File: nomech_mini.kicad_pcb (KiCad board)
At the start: 2 copper layers, 63 x 63 mm, 5 parts

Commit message: trying out LED position
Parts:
- added SM0603: Val**, SM0603, F.Cu at (138.1, 83.7)
- added SM0603: Val**, SM0603, F.Cu at (138.1, 95.8)
- added SM0603: Val**, SM0603, F.Cu at (150.3, 95.8)
- added SM0603: Val**, SM0603, F.Cu at (150.3, 83.7)

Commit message: starting schematic, adjusting pcb
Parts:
- added 80x80: 80mm, dp_pcb-DP8080_V1_drawing, F.Cu at (98.8, 154.8)
- DP10080_v1: renamed from 80mm; value 100mm -> 100x80mm
- moved MICRO-B_USB 95.6 mm to (80.2, 114.8), turned to 270 degrees
- moved TQFP44 70.4 mm to (96.2, 114.8)
- moved SM0603 31.0 mm to (107.1, 83.1)
- moved cap-electrode_10mm 31.0 mm to (113.2, 89.2)
- moved SM0603 31.0 mm to (107.1, 95.4)
- moved SM0603 30.9 mm to (119.4, 83.1)
- moved SM0603 30.9 mm to (119.4, 95.4)

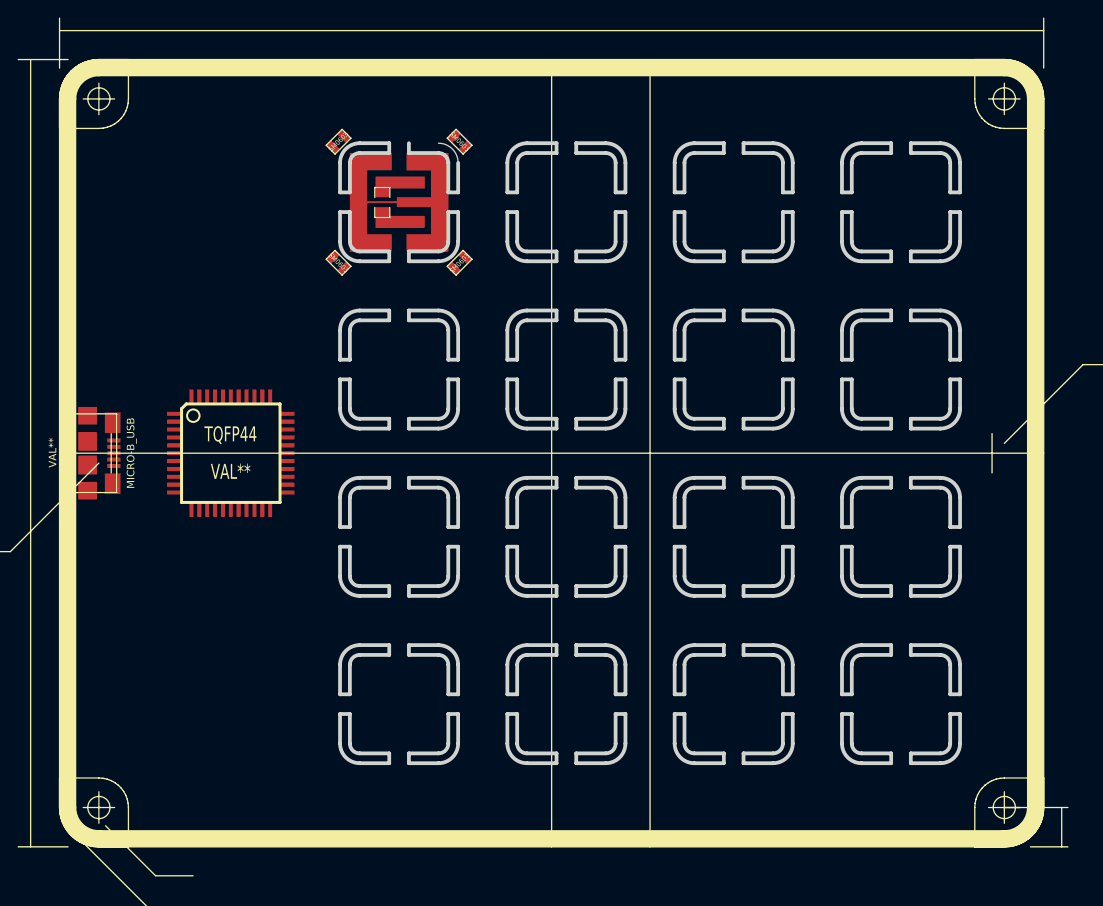
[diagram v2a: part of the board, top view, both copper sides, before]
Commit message: starting LED array, adjusting PCB
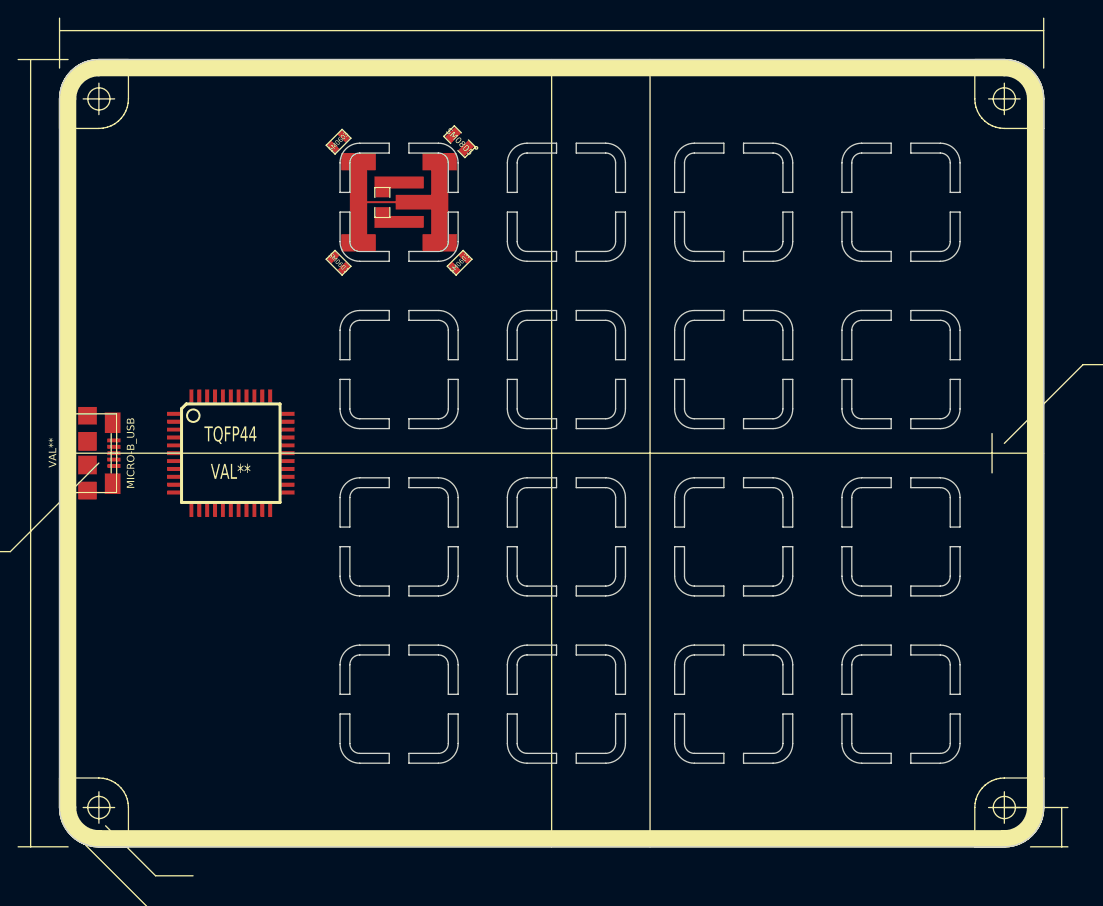
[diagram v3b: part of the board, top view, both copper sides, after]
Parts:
- SM0805: renamed from SM0603; footprint SM0603 -> SM0805
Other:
- board size 63 x 63 mm -> 100 x 80 mm

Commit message: working mainly on LEDs
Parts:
- moved cap-electrode_10mm 0.13 mm to (113.3, 89.1)
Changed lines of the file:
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@@
     (22 B.Mask user)
     (23 F.Mask user)
-    (24 Dwgs.User user hide)
+    (24 Dwgs.User user)
     (25 Cmts.User user)
     (26 Eco1.User user)
@@
   )
   (module cap-electrode_10mm (layer Front)
-    (at 113.25 89.25)
+    (at 113.3 89.125)
     (attr smd)
     (fp_text reference cap-electrode_10mm (at 0.1 6.4) (layer B.SilkS)

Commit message: messing about with elctrode
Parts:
- added cap-electrode_10mm: , cap-electrode_10mm, F.Cu at (113.1, 106.2)
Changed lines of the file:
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@@
     (tracks 0)
     (zones 0)
-    (modules 10)
+    (modules 11)
     (nets 1)
   )
@@
     (attr smd)
     (fp_text reference cap-electrode_10mm (at 0.1 6.4) (layer B.SilkS)
+      (effects (font (size 1.27 1.27) (thickness 0.0889)))
+    )
+    (fp_text value "" (at 0 0) (layer F.SilkS)
+      (effects (font (size 0.0004 0.0004) (thickness 0.00012)))
+    )
+    (fp_line (start -0.943 0.533) (end -0.943 1.549) (layer F.SilkS) (width 0.127))
+    (fp_line (start -0.943 1.549) (end -2.467 1.549) (layer F.SilkS) (width 0.127))
+    (fp_line (start -2.467 1.549) (end -2.467 0.533) (layer F.SilkS) (width 0.127))
+    (fp_line (start -2.467 -0.483) (end -2.467 -1.499) (layer F.SilkS) (width 0.127))
+    (fp_line (start -2.467 -1.499) (end -0.943 -1.499) (layer F.SilkS) (width 0.127))
+    (fp_line (start -0.943 -1.499) (end -0.943 -0.483) (layer F.SilkS) (width 0.127))
+    (pad 1 smd rect (at 4.125 4.125) (size 3.5 1.75)
+      (layers Front F.Mask)
+      (clearance 0.1)
+    )
+    (pad 1 smd rect (at 4.125 -4.125) (size 3.5 1.75)
+      (layers Front F.Mask)
+      (clearance 0.1)
+    )
+    (pad 1 smd rect (at -4.125 4.125) (size 3.5 1.75)
+      (layers Front F.Mask)
+      (clearance 0.1)
+    )
+    (pad 1 smd rect (at -4.125 0) (size 1.75 8.2)
+      (layers Front F.SilkS F.Mask)
+    )
+    (pad 1 smd rect (at 4.125 0) (size 1.75 8.2)
+      (layers Front F.SilkS F.Mask)
+    )
+    (pad 1 smd oval (at -4.125 -4.125) (size 1.75 1.75)
+      (layers Front F.Mask)
+    )
+    (pad 1 smd rect (at 2.15 0) (size 5 1.5)
+      (layers Front F.Mask)
+    )
+    (pad 2 smd rect (at 0 -2) (size 5 1.22)
+      (layers Front F.Mask)
+    )
+    (pad 2 smd rect (at 0 2) (size 5 1.22)
+      (layers Front F.Mask)
+    )
+    (pad 1 smd rect (at -1.45 0) (size 4.25 0.2)
+      (layers Front F.Mask)
+      (clearance 0.1)
+    )
+    (pad 2 smd rect (at -1.7 -0.95 90) (size 0.889 1.397)
+      (layers Front F.Paste F.Mask)
+    )
+    (pad 2 smd rect (at -1.7 0.95 90) (size 0.889 1.397)
+      (layers Front F.Paste F.Mask)
+    )
+    (pad 1 smd rect (at -4.125 -4.125) (size 3.5 1.75)
+      (layers Front F.Mask)
+      (clearance 0.1)
+    )
+    (pad 1 smd oval (at -4.125 4.125) (size 1.75 1.75)
+      (layers Front F.Mask)
+    )
+    (pad 1 smd oval (at 4.125 -4.125) (size 1.75 1.75)
+      (layers Front F.Mask)
+    )
+    (pad 1 smd oval (at 4.125 4.125) (size 1.75 1.75)
+      (layers Front F.Mask)
+    )
+  )
+  (module cap-electrode_10mm (layer Front)
+    (at 113.075 106.15)
+    (attr smd)
+    (fp_text reference cap-electrode_10mm (at 0.1 6.4) (layer B.SilkS)

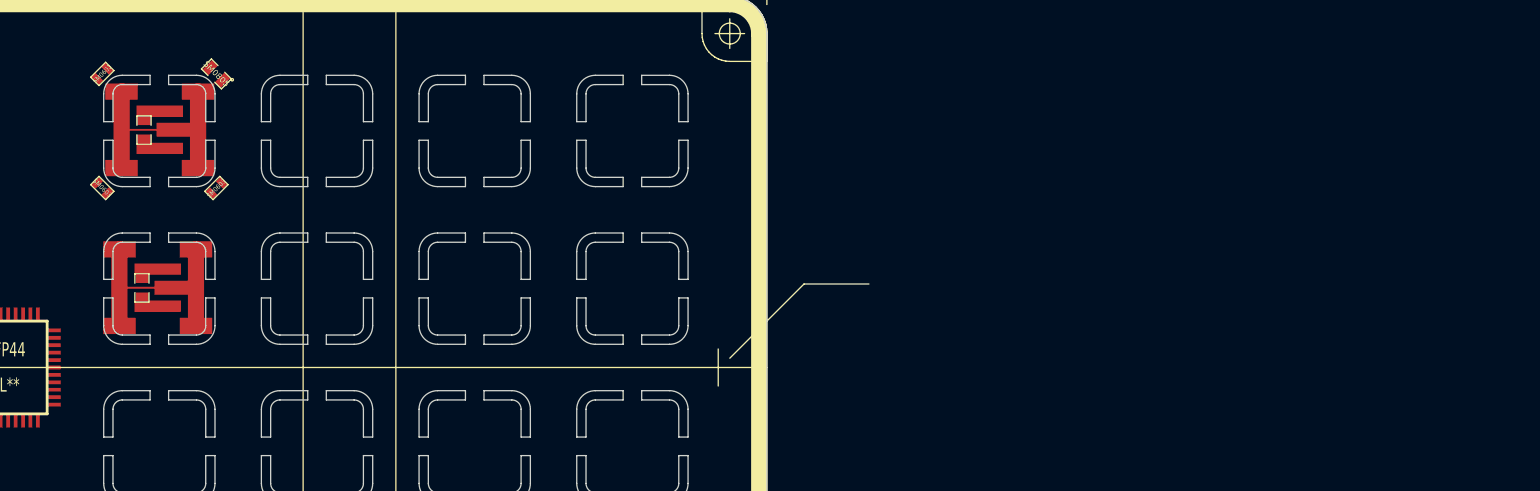
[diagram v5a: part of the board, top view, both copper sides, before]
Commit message: adding netlist, just for messing with footprints
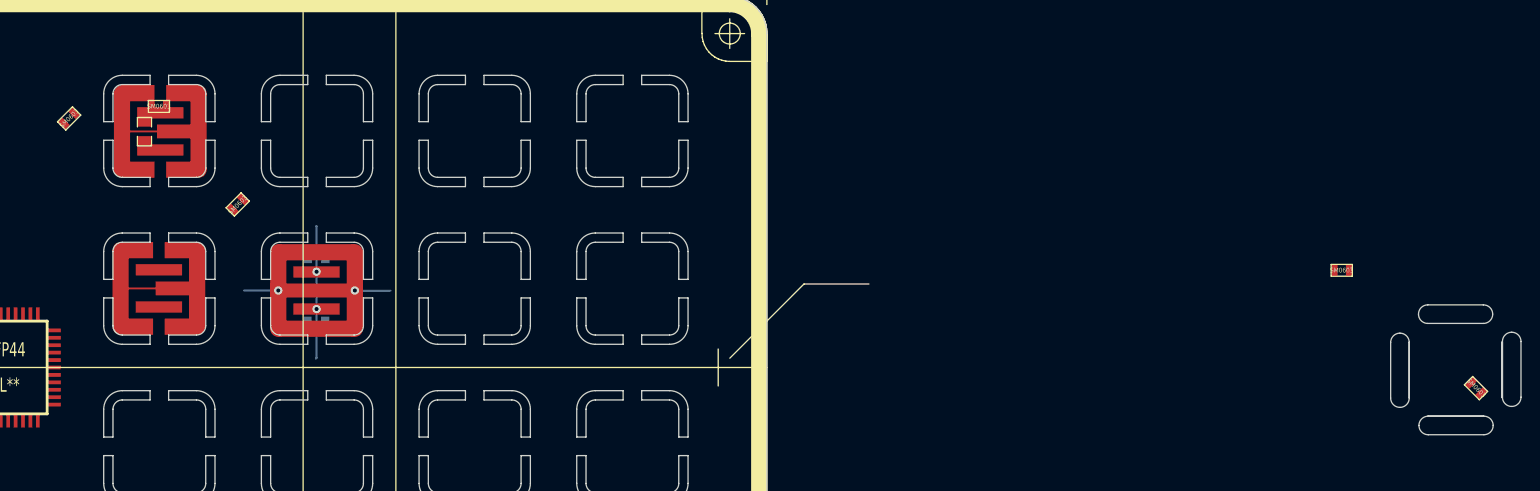
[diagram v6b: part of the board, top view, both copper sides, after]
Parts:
- removed the SM0603 at (107.1, 83.1)
- removed the SM0603 at (119.4, 95.4)
- removed the cap-electrode_10mm at (113.3, 89.1)
- removed the cap-electrode_10mm at (113.1, 106.2)
- added R4: R, cap-electrode_10mm_2layer, F.Cu at (130.2, 106.5)
- added SM0603: Val**, SM0603, F.Cu at (255.2, 117.0)
- added SM0603: Val**, SM0603, F.Cu at (113.2, 86.6)
- added SM0603: Val**, SM0603, F.Cu at (240.7, 104.3)
- added SM0603: Val**, SM0603, F.Cu at (121.7, 97.2)
- added SM0805: Val*, SM0805, B.Cu at (130.2, 102.8)
- added cap-electrode_10mm: , cap-electrode_10mm, F.Cu at (113.3, 89.3)
- added cap-electrode_10mm_2layer: , cap-electrode_10mm_2layer, F.Cu at (113.2, 106.2)
- SM0805: moved to B.Cu
- moved SM0805 29.0 mm to (130.2, 110.0), turned to 0 degrees
- moved SM0603 8.31 mm to (103.5, 87.9), turned to 225 degrees
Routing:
- net N-0000016: track 0.00 -> 44.7 mm, vias 0 -> 2
- net N-0000017: track 0.00 -> 14.4 mm, vias 0 -> 2
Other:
- board size 100 x 80 mm -> 152.8 x 63 mm

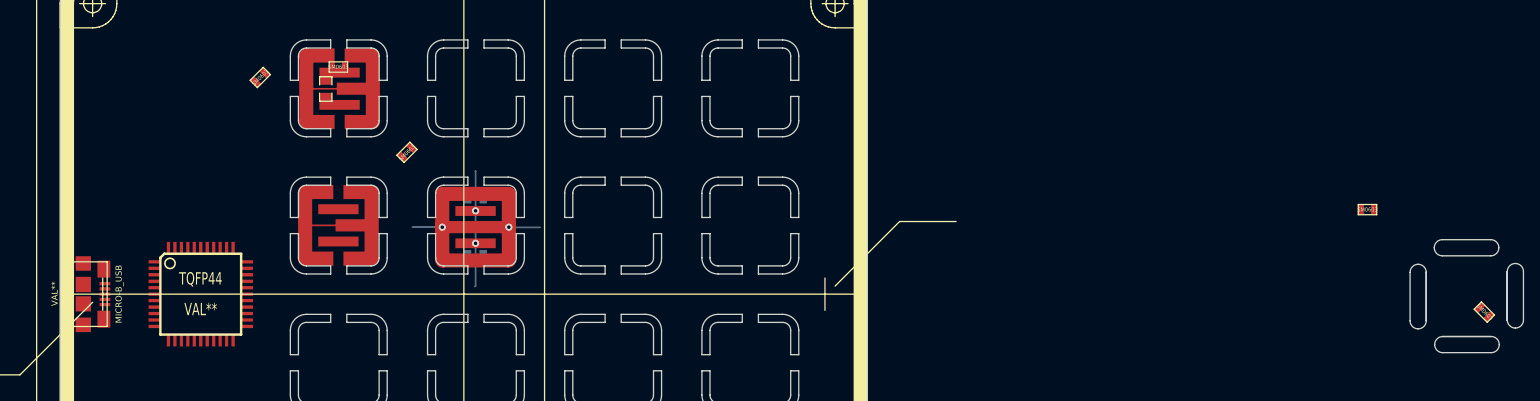
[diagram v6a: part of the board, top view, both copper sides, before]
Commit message: commiting before change to LED numbers
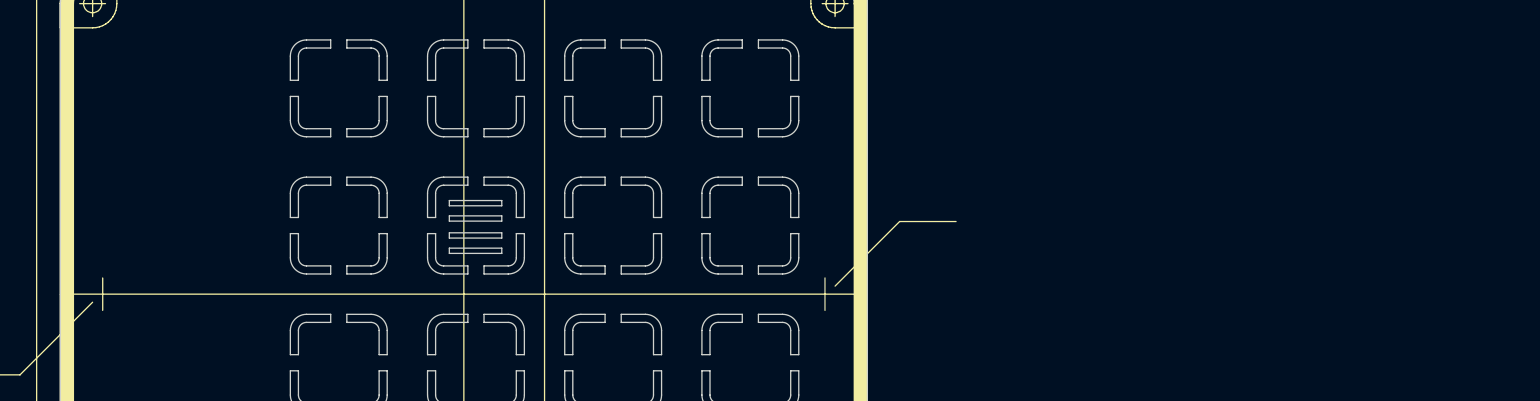
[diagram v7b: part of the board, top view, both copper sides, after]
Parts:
- removed MICRO-B_USB: VAL**, MICRO-B_USB
- removed R4: R, cap-electrode_10mm_2layer
- removed SM0603 (x5): Val**, SM0603
- removed SM0805: Val**, SM0805
- removed SM0805: Val*, SM0805
- removed TQFP44: VAL**, TQFP44
- removed cap-electrode_10mm: , cap-electrode_10mm
- removed cap-electrode_10mm_2layer: , cap-electrode_10mm_2layer
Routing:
- net N-0000016: track 44.7 -> 0.00 mm, vias 2 -> 0
- net N-0000017: track 14.4 -> 0.00 mm, vias 2 -> 0
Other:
- board size 152.8 x 63 mm -> 100 x 80 mm

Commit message: starting layout
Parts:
- removed STUB: VAL**, STUB
- added C1: 100nF, SM0805, B.Cu at (75.2, 225.6)
- added C10: 100nF, SM0805, B.Cu at (108.1, 225.6)
- added C11: 10nF, SM0805, B.Cu at (68.0, 225.6)
- added C12: 18pF, SM0805, B.Cu at (89.8, 225.6)
- added C13: 10nF, SM0805, B.Cu at (71.6, 225.6)
- added C14: 100nF, SM0805, B.Cu at (140.9, 225.6)
- added C15: 4.7nF, SM0805, B.Cu at (151.8, 225.2)
- added C16: 4.7nF, SM0805, B.Cu at (228.5, 225.9)
- added C17: 4.7nF, SM0805, B.Cu at (184.7, 225.9)
- added C18: 4.7nF, SM0805, B.Cu at (129.9, 225.6)
- added C2: 100nF, SM0805, B.Cu at (151.9, 222.8)
- added C3: 100nF, SM0805, B.Cu at (57.0, 225.6)
- added C4: 1uF, SM0805, B.Cu at (86.2, 225.6)
- added C5: 100nF, SM0805, B.Cu at (108.1, 227.9)
- added C6: 10nF, SM0805, B.Cu at (111.7, 225.6)
- added C7: 100nF, SM0805, B.Cu at (104.4, 225.6)
- added C8: 10nF, SM0805, B.Cu at (64.3, 225.6)
- added C9: 18pF, SM0805, B.Cu at (93.5, 225.6)
- added CON1: USB_2B, MICRO-B_USB, B.Cu at (139.2, 85.0)
- added CON2: AVR-ISP-6, pin_array_3x2, F.Cu at (164.0, 96.0)
- added D1: LED, KPJA-2107SURCK, B.Cu at (106.8, 111.2)
- added D10: LED, KPJA-2107SURCK, B.Cu at (71.8, 227.5)
- added D11: LED, KPJA-2107SURCK, B.Cu at (100.2, 227.5)
- added D12: LED, KPJA-2107SURCK, B.Cu at (81.3, 227.5)
- added D13: LED, KPJA-2107SURCK, B.Cu at (199.1, 242.2)
- added D14: LED, KPJA-2107SURCK, B.Cu at (227.6, 242.2)
- added D15: LED, KPJA-2107SURCK, B.Cu at (265.5, 242.2)
- added D16: LED, KPJA-2107SURCK, B.Cu at (213.3, 242.2)
- added D17: LED, KPJA-2107SURCK, B.Cu at (170.6, 242.2)
- added D18: LED, KPJA-2107SURCK, B.Cu at (76.5, 227.5)
- added D19: LED, KPJA-2107SURCK, B.Cu at (251.3, 242.2)
- added D2: LED, KPJA-2107SURCK, B.Cu at (120.8, 111.2)
- added D20: LED, KPJA-2107SURCK, B.Cu at (175.3, 242.2)
- added D21: LED, KPJA-2107SURCK, B.Cu at (203.8, 242.2)
- added D22: LED, KPJA-2107SURCK, B.Cu at (260.8, 242.2)
- added D23: LED, KPJA-2107SURCK, B.Cu at (246.5, 242.2)
- added D24: LED, KPJA-2107SURCK, B.Cu at (232.3, 242.2)
- added D25: LED, KPJA-2107SURCK, B.Cu at (218.1, 242.2)
- added D26: LED, KPJA-2107SURCK, B.Cu at (86.0, 227.5)
- added D27: LED, KPJA-2107SURCK, B.Cu at (90.8, 227.5)
- added D28: LED, KPJA-2107SURCK, B.Cu at (184.8, 242.2)
- added D29: LED, KPJA-2107SURCK, B.Cu at (222.8, 242.2)
- added D3: LED, KPJA-2107SURCK, B.Cu at (123.8, 125.2)
- added D30: LED, KPJA-2107SURCK, B.Cu at (67.0, 227.5)
- added D31: LED, KPJA-2107SURCK, B.Cu at (180.1, 242.2)
- added D32: LED, KPJA-2107SURCK, B.Cu at (241.8, 242.2)
- added D33: LED, KPJA-2107SURCK, B.Cu at (208.6, 242.2)
- added D4: LED, KPJA-2107SURCK, B.Cu at (137.8, 125.5)
- added D5: LED, KPJA-2107SURCK, B.Cu at (194.3, 242.2)
- added D6: LED, KPJA-2107SURCK, B.Cu at (256.0, 242.2)
- added D7: LED, KPJA-2107SURCK, B.Cu at (275.0, 242.2)
- added D8: LED, KPJA-2107SURCK, B.Cu at (189.6, 242.2)
- added D9: LED, KPJA-2107SURCK, B.Cu at (237.0, 242.2)
- added E1: CAP-ELECTRODE, cap-electrode_10mm_2layer, F.Cu at (113.8, 118.2)
- added E10: CAP-ELECTRODE, cap-electrode_10mm_2layer, F.Cu at (130.8, 152.2)
- added E11: CAP-ELECTRODE, cap-electrode_10mm_2layer, F.Cu at (147.8, 152.2)
- added E12: CAP-ELECTRODE, cap-electrode_10mm_2layer, F.Cu at (164.8, 152.2)
- added E13: CAP-ELECTRODE, cap-electrode_10mm_2layer, F.Cu at (113.8, 169.2)
- added E14: CAP-ELECTRODE, cap-electrode_10mm_2layer, F.Cu at (130.8, 169.2)
- added E15: CAP-ELECTRODE, cap-electrode_10mm_2layer, F.Cu at (147.8, 169.2)
- added E16: CAP-ELECTRODE, cap-electrode_10mm_2layer, F.Cu at (164.8, 169.2)
- added E2: CAP-ELECTRODE, cap-electrode_10mm_2layer, F.Cu at (130.8, 118.2)
- added E3: CAP-ELECTRODE, cap-electrode_10mm_2layer, F.Cu at (147.8, 118.2)
- added E4: CAP-ELECTRODE, cap-electrode_10mm_2layer, F.Cu at (164.8, 118.2)
- added E5: CAP-ELECTRODE, cap-electrode_10mm_2layer, F.Cu at (113.8, 135.2)
- added E6: CAP-ELECTRODE, cap-electrode_10mm_2layer, F.Cu at (130.8, 135.2)
- added E7: CAP-ELECTRODE, cap-electrode_10mm_2layer, F.Cu at (147.8, 135.2)
- added E8: CAP-ELECTRODE, cap-electrode_10mm_2layer, F.Cu at (164.8, 135.2)
- added E9: CAP-ELECTRODE, cap-electrode_10mm_2layer, F.Cu at (113.8, 152.2)
- added L1: FERRITE_BEAD, SM0805, B.Cu at (100.8, 225.6)
- added L2: FERRITE_BEAD, SM0805, B.Cu at (60.7, 225.6)
- added P2: CONN_1, PIN_ARRAY_1, F.Cu at (145.6, 208.1)
- added P3: CONN_1, PIN_ARRAY_1, F.Cu at (139.8, 208.1)
- added P4: CONN_1, PIN_ARRAY_1, F.Cu at (134.0, 208.1)
- added P5: CONN_1, PIN_ARRAY_1, F.Cu at (128.2, 208.1)
- added P6: CONN_1, PIN_ARRAY_1, F.Cu at (167.5, 102.8)
- added Q1: MOSFET_N, SOT23-NX7002AK, B.Cu at (166.6, 241.6)
- added Q2: MOSFET_N, SOT23-NX7002AK, B.Cu at (163.5, 241.6)
- added Q3: MOSFET_N, SOT23-NX7002AK, B.Cu at (157.2, 241.6)
- added Q4: MOSFET_N, SOT23-NX7002AK, B.Cu at (160.3, 241.6)
- added R1: 10k, SM0805, B.Cu at (97.1, 225.6)
- added R10: 1M, SM0805, B.Cu at (177.4, 225.9)
- added R11: 1M, SM0805, B.Cu at (144.6, 225.6)
- added R12: 1M, SM0805, B.Cu at (133.6, 225.6)
- added R13: 1k, SM0805, B.Cu at (159.1, 223.6)
- added R14: 1k, SM0805, B.Cu at (181.1, 225.9)
- added R15: 1k, SM0805, B.Cu at (148.2, 225.6)
- added R16: 1k, SM0805, B.Cu at (137.2, 225.6)
- added R17: 22R, SM0805, B.Cu at (206.6, 225.9)
- added R18: 22R, SM0805, B.Cu at (199.3, 225.9)
- added R19: 22R, SM0805, B.Cu at (224.8, 225.9)
- added R2: 22R, SM0805, B.Cu at (78.9, 225.6)
- added R20: 22R, SM0805, B.Cu at (192.0, 225.9)
- added R21: 4k7, SM0805, B.Cu at (210.2, 225.9)
- added R22: 4k7, SM0805, B.Cu at (202.9, 225.9)
- added R23: 4k7, SM0805, B.Cu at (188.3, 225.9)
- added R24: 4k7, SM0805, B.Cu at (195.7, 225.9)
- added R25: 120R, SM0805, B.Cu at (213.9, 225.9)
- added R26: 120R, SM0805, B.Cu at (173.8, 225.9)
- added R27: 120R, SM0805, B.Cu at (243.1, 225.9)
- added R28: 120R, SM0805, B.Cu at (257.6, 225.9)
- added R29: 120R, SM0805, B.Cu at (144.6, 227.9)
- added R3: 22R, SM0805, B.Cu at (82.5, 225.6)
- added R30: 120R, SM0805, B.Cu at (159.2, 225.9)
- added R31: 120R, SM0805, B.Cu at (111.8, 227.9)
- added R32: 120R, SM0805, B.Cu at (130.0, 227.9)
- added R33: 120R, SM0805, B.Cu at (217.5, 225.9)
- added R34: 120R, SM0805, B.Cu at (232.1, 225.9)
- added R35: 120R, SM0805, B.Cu at (246.7, 225.9)
- added R36: 120R, SM0805, B.Cu at (261.3, 225.9)
- added R37: 120R, SM0805, B.Cu at (170.1, 225.9)
- added R38: 120R, SM0805, B.Cu at (155.5, 225.9)
- added R39: 120R, SM0805, B.Cu at (140.9, 227.9)
- added R4: 120R, SM0805, B.Cu at (104.5, 227.9)
- added R40: 120R, SM0805, B.Cu at (126.3, 227.9)
- added R41: 120R, SM0805, B.Cu at (221.2, 225.9)
- added R42: 120R, SM0805, B.Cu at (235.8, 225.9)
- added R43: 120R, SM0805, B.Cu at (250.3, 225.9)
- added R44: 120R, SM0805, B.Cu at (264.9, 225.9)
- added R45: 120R, SM0805, B.Cu at (166.5, 225.9)
- added R46: 120R, SM0805, B.Cu at (115.4, 227.9)
- added R47: 120R, SM0805, B.Cu at (137.3, 227.9)
- added R48: 120R, SM0805, B.Cu at (122.7, 227.9)
- added R49: 120R, SM0805, B.Cu at (268.6, 225.9)
- added R5: 1k, SM0805, B.Cu at (126.3, 225.6)
- added R50: 120R, SM0805, B.Cu at (239.4, 225.9)
- added R51: 120R, SM0805, B.Cu at (254.0, 225.9)
- added R52: 120R, SM0805, B.Cu at (272.2, 225.9)
- added R53: 120R, SM0805, B.Cu at (162.8, 225.9)
- added R54: 120R, SM0805, B.Cu at (148.2, 227.9)
- added R55: 120R, SM0805, B.Cu at (133.7, 227.9)
- added R56: 120R, SM0805, B.Cu at (119.1, 227.9)
- added R6: 1k, SM0805, B.Cu at (122.7, 225.6)
- added R7: 1k, SM0805, B.Cu at (119.0, 225.6)
- added R8: 1k, SM0805, B.Cu at (115.4, 225.6)
- added R9: 1M, SM0805, B.Cu at (155.5, 223.6)
- added U1: ATMEGA32U4, TQFP44, B.Cu at (121.0, 98.5)
- added X1: CRYSTAL_16MHz, adafruit-NX5032, B.Cu at (111.0, 98.0)
- moved DP10080_v1 73.9 mm to (99.2, 83.8), turned to 270 degrees
- moved 80x80 51.0 mm to (99.2, 103.8), turned to 270 degrees
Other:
- board size 100 x 80 mm -> 80 x 100 mm
